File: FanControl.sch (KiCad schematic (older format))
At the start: 4 parts

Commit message: Updated TR3 foor print and re-routed tracks.
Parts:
- D12: footprint Diode_SMD:D_SOD-323F -> Diode_SMD:D_SOD-323_HandSoldering
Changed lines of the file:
@@
 AR Path="/5AB91A68/5AB906E9" Ref="#PWR073"  Part="1"
 AR Path="/5AB91A71/5AB906E9" Ref="#PWR074"  Part="1"
-F 0 "#PWR074" H 5250 3750 50  0001 C CNN
+F 0 "#PWR071" H 5250 3750 50  0001 C CNN
 F 1 "GND" H 5255 3827 50  0000 C CNN
 F 2 "" H 5250 4000 50  0001 C CNN
@@
 F 0 "D12" V 5204 2529 50  0000 L CNN
 F 1 "1N4148" V 5295 2529 50  0000 L CNN
-F 2 "Diode_SMD:D_SOD-323F" H 5250 2450 50  0001 C CNN
+F 2 "Diode_SMD:D_SOD-323_HandSoldering" H 5250 2450 50  0001 C CNN
 F 3 "~" H 5250 2450 50  0001 C CNN
 	1    5250 2450

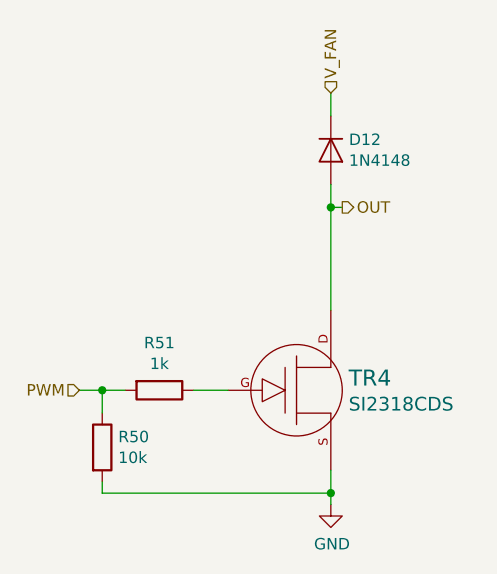
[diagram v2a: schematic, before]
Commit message: Added 10k pullups to control inputs for heaters, to disable heaters when control module is not installed.
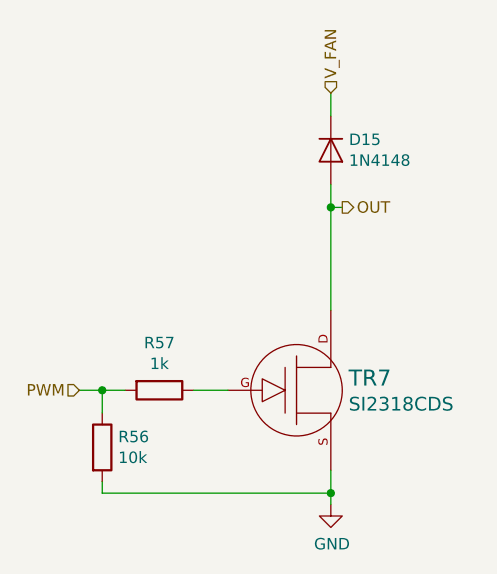
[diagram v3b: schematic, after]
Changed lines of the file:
@@
 AR Path="/5AB91A68/5AB90282" Ref="R55"  Part="1"
 AR Path="/5AB91A71/5AB90282" Ref="R57"  Part="1"
-F 0 "R51" V 4293 3500 50  0000 C CNN
+F 0 "R57" V 4293 3500 50  0000 C CNN
 F 1 "1k" V 4384 3500 50  0000 C CNN
 F 2 "Resistor_SMD:R_0603_1608Metric" V 4430 3500 50  0001 C CNN
@@
 AR Path="/5AB91A68/5AB906E9" Ref="#PWR073"  Part="1"
 AR Path="/5AB91A71/5AB906E9" Ref="#PWR074"  Part="1"
-F 0 "#PWR071" H 5250 3750 50  0001 C CNN
+F 0 "#PWR074" H 5250 3750 50  0001 C CNN
 F 1 "GND" H 5255 3827 50  0000 C CNN
 F 2 "" H 5250 4000 50  0001 C CNN
@@
 AR Path="/5AB91A68/5AB90621" Ref="TR6"  Part="1"
 AR Path="/5AB91A71/5AB90621" Ref="TR7"  Part="1"
-F 0 "TR4" H 5328 3553 70  0000 L CNN
+F 0 "TR7" H 5328 3553 70  0000 L CNN
 F 1 "SI2318CDS" H 5328 3439 60  0000 L CNN
 F 2 "PrntrBoardV1:SOT-23" H 5100 3500 60  0001 C CNN
@@
 AR Path="/5AB91A68/5AB969B0" Ref="R54"  Part="1"
 AR Path="/5AB91A71/5AB969B0" Ref="R56"  Part="1"
-F 0 "R50" H 4320 3796 50  0000 L CNN
+F 0 "R56" H 4320 3796 50  0000 L CNN
 F 1 "10k" H 4320 3705 50  0000 L CNN
 F 2 "Resistor_SMD:R_0603_1608Metric" V 4180 3750 50  0001 C CNN
@@
 AR Path="/5AB91A68/5AB96AD6" Ref="D14"  Part="1"
 AR Path="/5AB91A71/5AB96AD6" Ref="D15"  Part="1"
-F 0 "D12" V 5204 2529 50  0000 L CNN
+F 0 "D15" V 5204 2529 50  0000 L CNN
 F 1 "1N4148" V 5295 2529 50  0000 L CNN
 F 2 "Diode_SMD:D_SOD-323_HandSoldering" H 5250 2450 50  0001 C CNN

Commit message: Switch away from rounded rect pads. The PCB boar house had issues making the board.
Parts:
- R50, R51: footprint Resistor_SMD:R_0603_1608Metric -> PrntrBoardV1:R_0603_1608Metric
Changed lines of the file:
@@
 F 0 "R57" V 4293 3500 50  0000 C CNN
 F 1 "1k" V 4384 3500 50  0000 C CNN
-F 2 "Resistor_SMD:R_0603_1608Metric" V 4430 3500 50  0001 C CNN
+F 2 "PrntrBoardV1:R_0603_1608Metric" V 4430 3500 50  0001 C CNN
 F 3 "~" H 4500 3500 50  0001 C CNN
 	1    4500 3500
@@
 F 0 "R56" H 4320 3796 50  0000 L CNN
 F 1 "10k" H 4320 3705 50  0000 L CNN
-F 2 "Resistor_SMD:R_0603_1608Metric" V 4180 3750 50  0001 C CNN
+F 2 "PrntrBoardV1:R_0603_1608Metric" V 4180 3750 50  0001 C CNN
 F 3 "~" H 4250 3750 50  0001 C CNN
 	1    4250 3750

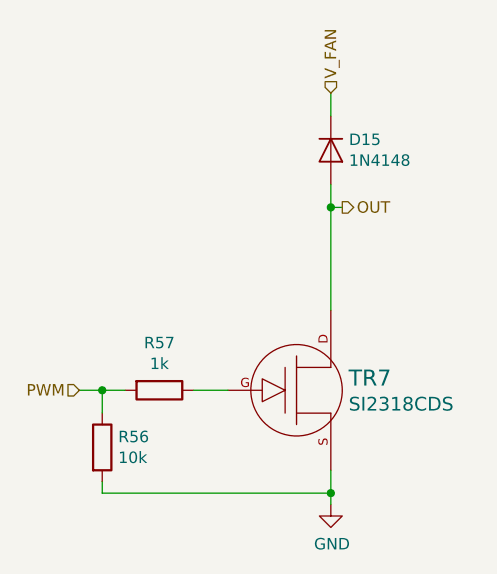
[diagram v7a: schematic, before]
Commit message: Fix bug in the TMC2130 driver schematics.
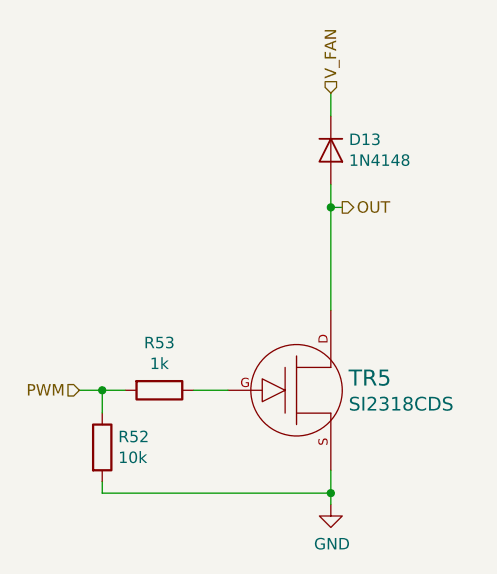
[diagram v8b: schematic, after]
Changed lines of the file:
@@
 EESchema Schematic File Version 5
-LIBS:PrntrBoardV1-cache
-EELAYER 29 0
+EELAYER 34 0
 EELAYER END
 $Descr A4 11693 8268
@@
 Comment3 ""
 Comment4 ""
+Comment5 ""
+Comment6 ""
+Comment7 ""
+Comment8 ""
+Comment9 ""
 $EndDescr
+Connection ~ 4250 3500
+Connection ~ 5250 3950
+Connection ~ 5250 2700
+Wire Wire Line
+	4250 3500 4150 3500
+Wire Wire Line
+	4250 3600 4250 3500
+Wire Wire Line
+	4250 3900 4250 3950
+Wire Wire Line
+	4250 3950 5250 3950
+Wire Wire Line
+	4350 3500 4250 3500
+Wire Wire Line
+	4800 3500 4650 3500
+Wire Wire Line
+	5250 2200 5250 2300
+Wire Wire Line
+	5250 2600 5250 2700
+Wire Wire Line
+	5250 2700 5250 3150
+Wire Wire Line
+	5250 2700 5300 2700
+Wire Wire Line
+	5250 3850 5250 3950
+Wire Wire Line
+	5250 3950 5250 4000
+Text HLabel 4150 3500 0    50   Input ~ 0
+PWM
+Text HLabel 5250 2200 1    50   Input ~ 0
+V_FAN
+Text HLabel 5300 2700 2    50   Output ~ 0
+OUT
+$Comp
+L power:GND #PWR071
+U 1 1 5AB906E9
+P 5250 4000
+AR Path="/5AB9002A/5AB906E9" Ref="#PWR071"  Part="1"
+AR Path="/5AB91A5D/5AB906E9" Ref="#PWR072"  Part="1"
+AR Path="/5AB91A68/5AB906E9" Ref="#PWR073"  Part="1"
+AR Path="/5AB91A71/5AB906E9" Ref="#PWR074"  Part="1"
+F 0 "#PWR072" H 5250 3750 50  0001 C CNN
+F 1 "GND" H 5255 3827 50  0000 C CNN
+F 2 "" H 5250 4000 50  0001 C CNN
+F 3 "" H 5250 4000 50  0001 C CNN
+	1    5250 4000
+	1    0    0    -1
+$EndComp
+$Comp
+L Device:R R50
+U 1 1 5AB969B0
+P 4250 3750
+AR Path="/5AB9002A/5AB969B0" Ref="R50"  Part="1"
+AR Path="/5AB91A5D/5AB969B0" Ref="R52"  Part="1"
+AR Path="/5AB91A68/5AB969B0" Ref="R54"  Part="1"
+AR Path="/5AB91A71/5AB969B0" Ref="R56"  Part="1"
+F 0 "R52" H 4320 3796 50  0000 L CNN
+F 1 "10k" H 4320 3705 50  0000 L CNN
+F 2 "PrntrBoardV1:R_0603_1608Metric" V 4180 3750 50  0001 C CNN
+F 3 "~" H 4250 3750 50  0001 C CNN
+	1    4250 3750
+	1    0    0    -1
+$EndComp
 $Comp
 L Device:R R51
@@
 AR Path="/5AB91A68/5AB90282" Ref="R55"  Part="1"
 AR Path="/5AB91A71/5AB90282" Ref="R57"  Part="1"
-F 0 "R57" V 4293 3500 50  0000 C CNN
+F 0 "R53" V 4293 3500 50  0000 C CNN
 F 1 "1k" V 4384 3500 50  0000 C CNN
 F 2 "PrntrBoardV1:R_0603_1608Metric" V 4430 3500 50  0001 C CNN
@@
 $EndComp
 $Comp
-L power:GND #PWR071
-U 1 1 5AB906E9
-P 5250 4000
-AR Path="/5AB9002A/5AB906E9" Ref="#PWR071"  Part="1"
-AR Path="/5AB91A5D/5AB906E9" Ref="#PWR072"  Part="1"
-AR Path="/5AB91A68/5AB906E9" Ref="#PWR073"  Part="1"
-AR Path="/5AB91A71/5AB906E9" Ref="#PWR074"  Part="1"
-F 0 "#PWR074" H 5250 3750 50  0001 C CNN
-F 1 "GND" H 5255 3827 50  0000 C CNN
-F 2 "" H 5250 4000 50  0001 C CNN
-F 3 "" H 5250 4000 50  0001 C CNN
-	1    5250 4000
-	1    0    0    -1
+L Device:D D12
+U 1 1 5AB96AD6
+P 5250 2450
+AR Path="/5AB9002A/5AB96AD6" Ref="D12"  Part="1"
+AR Path="/5AB91A5D/5AB96AD6" Ref="D13"  Part="1"
+AR Path="/5AB91A68/5AB96AD6" Ref="D14"  Part="1"
+AR Path="/5AB91A71/5AB96AD6" Ref="D15"  Part="1"
+F 0 "D13" V 5204 2529 50  0000 L CNN
+F 1 "1N4148" V 5295 2529 50  0000 L CNN
+F 2 "Diode_SMD:D_SOD-323_HandSoldering" H 5250 2450 50  0001 C CNN
+F 3 "~" H 5250 2450 50  0001 C CNN
+	1    5250 2450
+	0    1    1    0
 $EndComp
-Wire Wire Line
-	4800 3500 4650 3500
-Wire Wire Line
-	5250 3850 5250 3950
-Wire Wire Line
-	4350 3500 4250 3500
-Wire Wire Line
-	5250 2700 5300 2700
-Text HLabel 5300 2700 2    50   Output ~ 0
-OUT
-Text HLabel 4150 3500 0    50   Input ~ 0
-PWM
-Text HLabel 5250 2200 1    50   Input ~ 0
-V_FAN
 $Comp
 L bsh105:BSH105 TR4
@@
 AR Path="/5AB91A68/5AB90621" Ref="TR6"  Part="1"
 AR Path="/5AB91A71/5AB90621" Ref="TR7"  Part="1"
-F 0 "TR7" H 5328 3553 70  0000 L CNN
+F 0 "TR5" H 5328 3553 70  0000 L CNN
 F 1 "SI2318CDS" H 5328 3439 60  0000 L CNN
 F 2 "PrntrBoardV1:SOT-23" H 5100 3500 60  0001 C CNN
@@
 	1    0    0    -1
 $EndComp
-Wire Wire Line
-	5250 2700 5250 3150
-$Comp
-L Device:R R50
-U 1 1 5AB969B0
-P 4250 3750
-AR Path="/5AB9002A/5AB969B0" Ref="R50"  Part="1"
-AR Path="/5AB91A5D/5AB969B0" Ref="R52"  Part="1"
-AR Path="/5AB91A68/5AB969B0" Ref="R54"  Part="1"
-AR Path="/5AB91A71/5AB969B0" Ref="R56"  Part="1"
-F 0 "R56" H 4320 3796 50  0000 L CNN
-F 1 "10k" H 4320 3705 50  0000 L CNN
-F 2 "PrntrBoardV1:R_0603_1608Metric" V 4180 3750 50  0001 C CNN
-F 3 "~" H 4250 3750 50  0001 C CNN
-	1    4250 3750
-	1    0    0    -1
-$EndComp
-Wire Wire Line
-	4250 3600 4250 3500
-Connection ~ 4250 3500
-Wire Wire Line
-	4250 3500 4150 3500
-Wire Wire Line
-	4250 3900 4250 3950
-Wire Wire Line
-	4250 3950 5250 3950
-Connection ~ 5250 3950
-Wire Wire Line
-	5250 3950 5250 4000
-$Comp
-L Device:D D12
-U 1 1 5AB96AD6
-P 5250 2450
-AR Path="/5AB9002A/5AB96AD6" Ref="D12"  Part="1"
-AR Path="/5AB91A5D/5AB96AD6" Ref="D13"  Part="1"
-AR Path="/5AB91A68/5AB96AD6" Ref="D14"  Part="1"
-AR Path="/5AB91A71/5AB96AD6" Ref="D15"  Part="1"
-F 0 "D15" V 5204 2529 50  0000 L CNN
-F 1 "1N4148" V 5295 2529 50  0000 L CNN
-F 2 "Diode_SMD:D_SOD-323_HandSoldering" H 5250 2450 50  0001 C CNN
-F 3 "~" H 5250 2450 50  0001 C CNN
-	1    5250 2450
-	0    1    1    0
-$EndComp
-Wire Wire Line
-	5250 2200 5250 2300
-Wire Wire Line
-	5250 2600 5250 2700
-Connection ~ 5250 2700
 $EndSCHEMATC
